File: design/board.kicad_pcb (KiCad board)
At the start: 2 copper layers, 96.5 x 81.3 mm, 14 parts, among them J1 Mic, J2 DEBUG_CONN, J3 PWR_CONN, J4 0.97" OLED, J5 WS2812b, SW1 SW_Push, U1 NodeMCU1.0(ESP-12E), U2 BME280

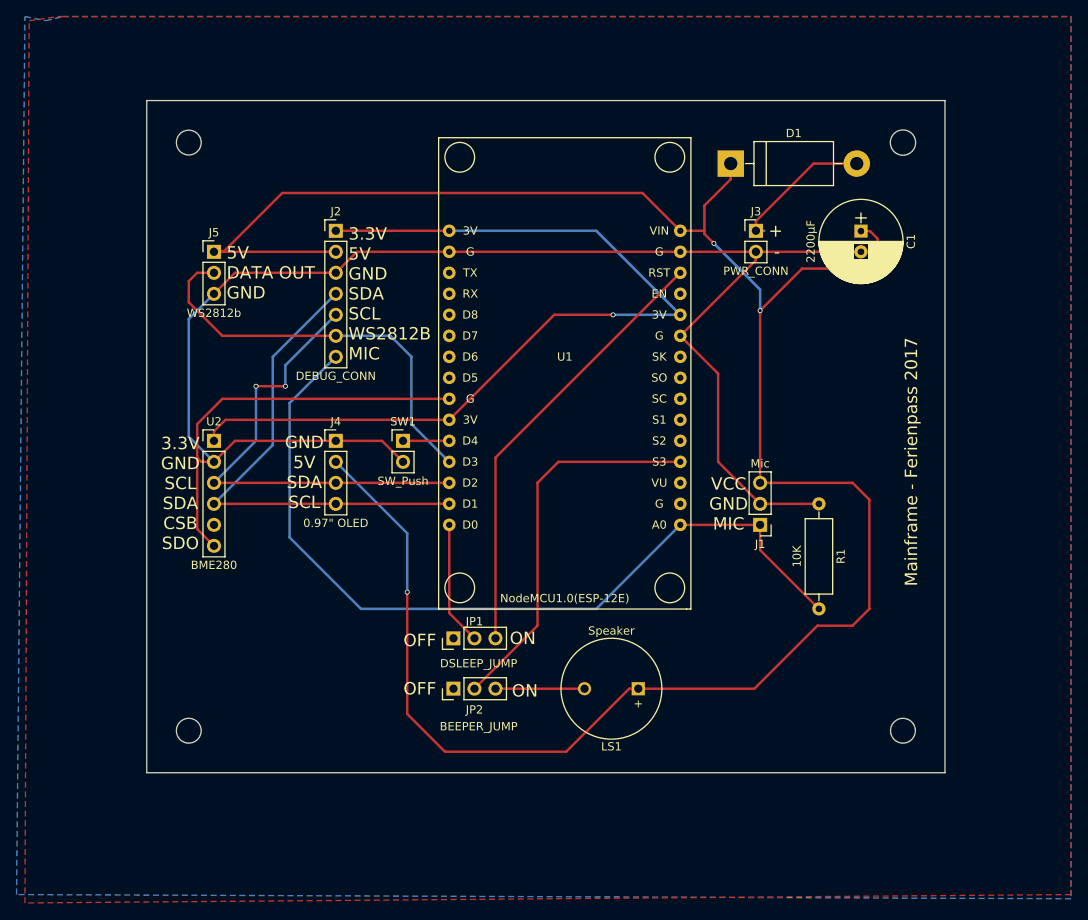
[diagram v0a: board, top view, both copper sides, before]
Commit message: correction of the Nodemcu Footprint
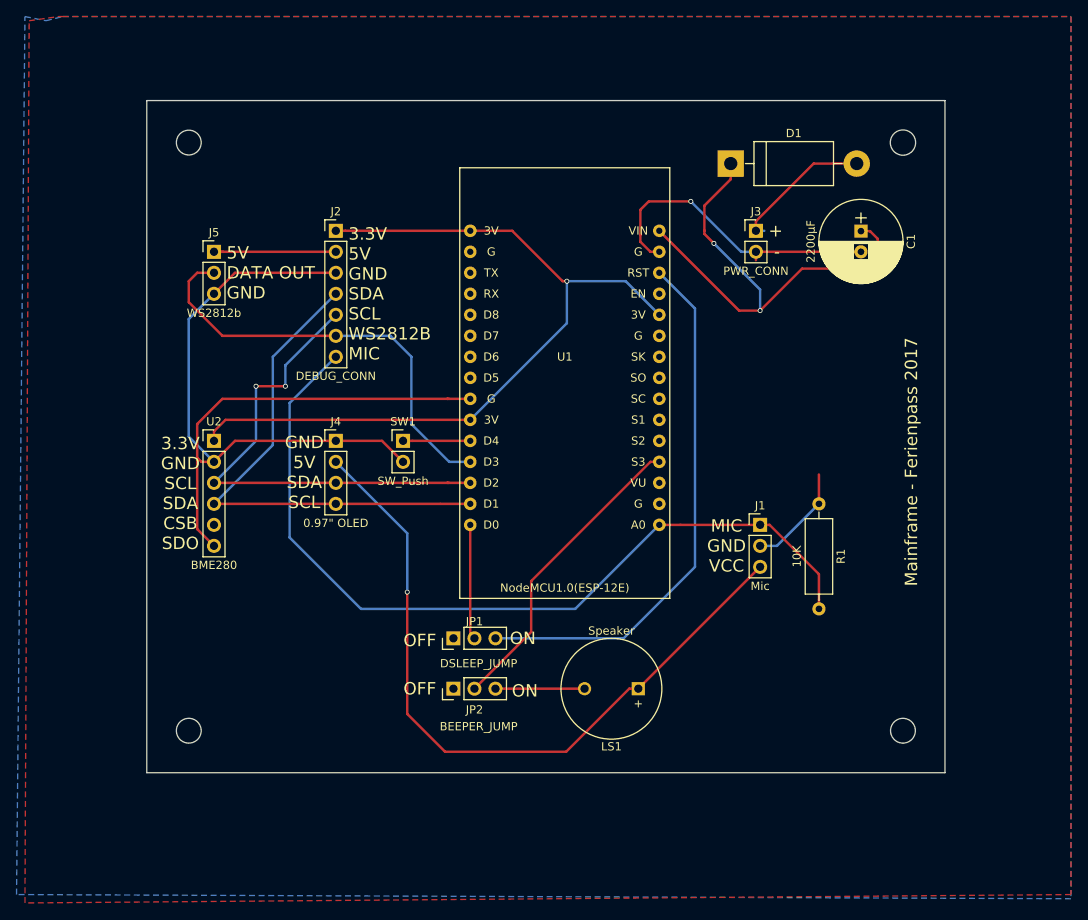
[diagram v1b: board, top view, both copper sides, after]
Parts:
- turned J1 to 0 degrees
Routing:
- net VCC: track 269.3 -> 163.4 mm
- net GND: track 223.1 -> 166.1 mm, vias 0 -> 1
- net Net-(JP1-Pad3): track 53.5 -> 65.1 mm
- net +3V3: track 109.2 -> 97.6 mm
- net SD3: track 46.4 -> 37.3 mm
- net SCL: track 57.0 -> 59.7 mm
- net SDA: track 60.0 -> 62.5 mm
- net WS2812b: track 50.3 -> 52.8 mm
- net Net-(SW1-Pad1): track 5.59 -> 8.13 mm
- net D0: track 15.0 -> 13.9 mm
- net MIC: track 101.9 -> 102.6 mm
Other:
- board text added: "MIC GND VCC"
- board text removed: "VCC GND MIC"

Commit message: improved PCB-Layout for next Year
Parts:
- SW1: footprint Pin_Headers:Pin_Header_Straight_1x02_Pitch2.54mm -> Socket_Strips:Socket_Strip_Straight_1x02_Pitch2.54mm
- moved D1 92.7 mm to (25.7, 88.6), turned to 90 degrees
- moved J3 77.4 mm to (25.7, 67.3), turned to 180 degrees
- moved LS1 67.9 mm to (47.4, 26.7)
- moved J1 67.6 mm to (28.2, 53.1)
- moved J5 66.8 mm to (63.0, 90.7), turned to 90 degrees
- moved JP2 66.0 mm to (29.2, 26.7)
- moved R1 63.4 mm to (44.5, 36.6), turned to 180 degrees
- moved C1 51.1 mm to (55.6, 34.0), turned to 0 degrees
- moved J2 47.0 mm to (63.5, 73.4), turned to 180 degrees
- moved U2 42.4 mm to (67.8, 72.1), turned to 180 degrees
- moved JP1 41.1 mm to (46.5, 40.6), turned to 270 degrees
- moved U1 37.0 mm to (45.7, 73.4), turned to 0 degrees
- moved J4 27.2 mm to (67.8, 45.0), turned to 180 degrees
- moved SW1 18.2 mm to (63.5, 42.9), turned to 180 degrees
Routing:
- net MIC: track 102.6 -> 53.9 mm, vias 0 -> 1
- net +3V3: track 97.6 -> 74.7 mm, vias 1 -> 0
- net SCL: track 59.7 -> 37.3 mm, vias 2 -> 0
- net SDA: track 62.5 -> 41.8 mm
- net Net-(JP1-Pad3): track 65.1 -> 46.9 mm
- net WS2812b: track 52.8 -> 36.2 mm
- net Net-(SW1-Pad1): track 8.13 -> 23.6 mm
- net Net-(D1-Pad2): track 17.2 -> 6.10 mm
- net D0: track 13.9 -> 20.9 mm
- net VCC: track 163.4 -> 168.7 mm, vias 3 -> 0
- net Net-(JP2-Pad3): track 10.8 -> 6.60 mm
- net SD3: track 37.3 -> 35.1 mm
- net GND: track 166.1 -> 164.0 mm, vias 1 -> 0
- removed copper zone on F.Cu, net GND
- removed copper zone on B.Cu, net VCC
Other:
- board size 96.5 x 81.3 mm -> 50 x 80 mm
- board text added: "Ferienpass 2018 KtT e.V."
- board text removed: "+"
- board text removed: "-"
- board text removed: "3.3V 5V GND SDA SCL WS2812B MIC"
- board text removed: "3.3V GND SCL SDA CSB SDO"
- board text removed: "5V DATA OUT GND"
- board text removed: "GND 5V SDA SCL"
- board text removed: "MIC GND VCC"
- board text removed: "Mainframe - Ferienpass 2017"
- board text removed: "OFF"
- board text removed: "ON"
